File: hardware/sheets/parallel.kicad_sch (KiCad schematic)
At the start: 18 parts, among them J1 DB25_Pins, U1 74HCT374, U10 74HCT32, U11 74HCT32, U2 74HCT374, U3 74HCT244, U4 74HCT245, U5 74HCT244, U6 74HCT138, U7 74HCT08, U8 74HCT08, U9 74HCT04

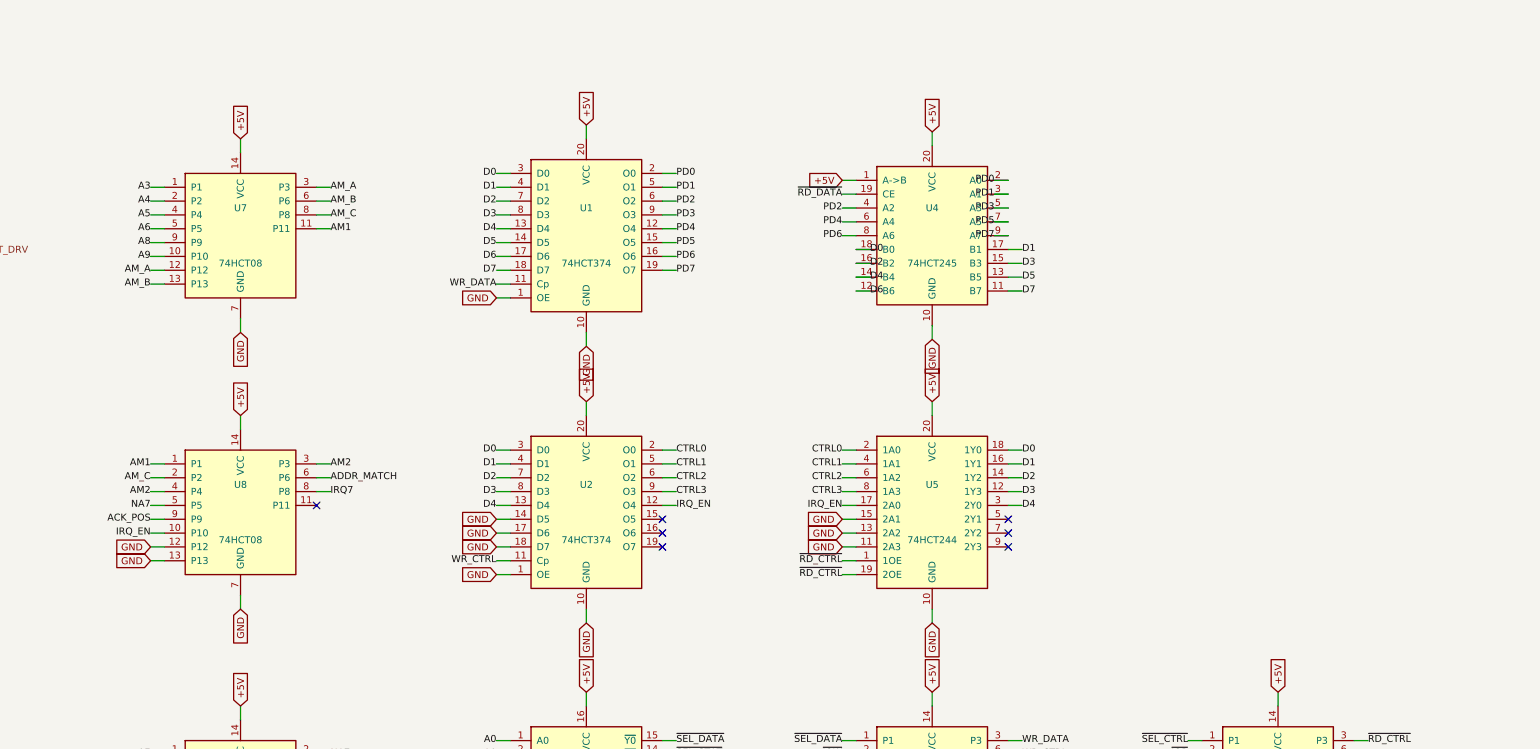
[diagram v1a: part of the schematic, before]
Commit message: Fix all low-severity + toolchain design-review findings
Low:
- LPT IRQ7 via tri-state '125 (NAND-enabled ack pulse) - shareable line
- card_com JP2 IRQ strap follows the base-address strap (was IRQ4-only)
- Supervisor USB-A VBUS fused (500mA polyfuse)
- card_isatest: DUT_PWR_EN moved to the control '595 (addr shifts can't
  glitch DUT power); '165s -> 74HC grade (HCT needs VCC 4.5-5.5V)
- /3 duty comments corrected; U13 marked load-bearing inverting buffer
- RTC AS hold-path bench note; duplicate ~RD stub removed
- mxbus PRIV_DECODE emptied (Y5 never leaves cpu_core)

Toolchain:
- build.py/build_cards return real exit codes, failing on structural ERC
  (endpoint_off_grid/unconnected_wire_endpoint/multiple_net_names) or a
  failed netlist export
- KiCad paths resolved via mxsch.kicad_cli()/kicad_symdir() (env, PATH,
  snap `current`) - no pinned snap revision anywhere
- Deterministic UUIDs (uuid5 title-seed + counter): rebuilds are
  byte-identical (verified); this rewrites every UUID once
- S-expression string escapes now round-trip (parse decodes, dump encodes)
- CLAUDE.md updated to match

The new structural gate immediately caught its own batch's bug (pull row
placed inside card_isatest's J2 pin field) - moved and re-verified.

Co-Authored-By: Claude Fable 5 <noreply@anthropic.com>
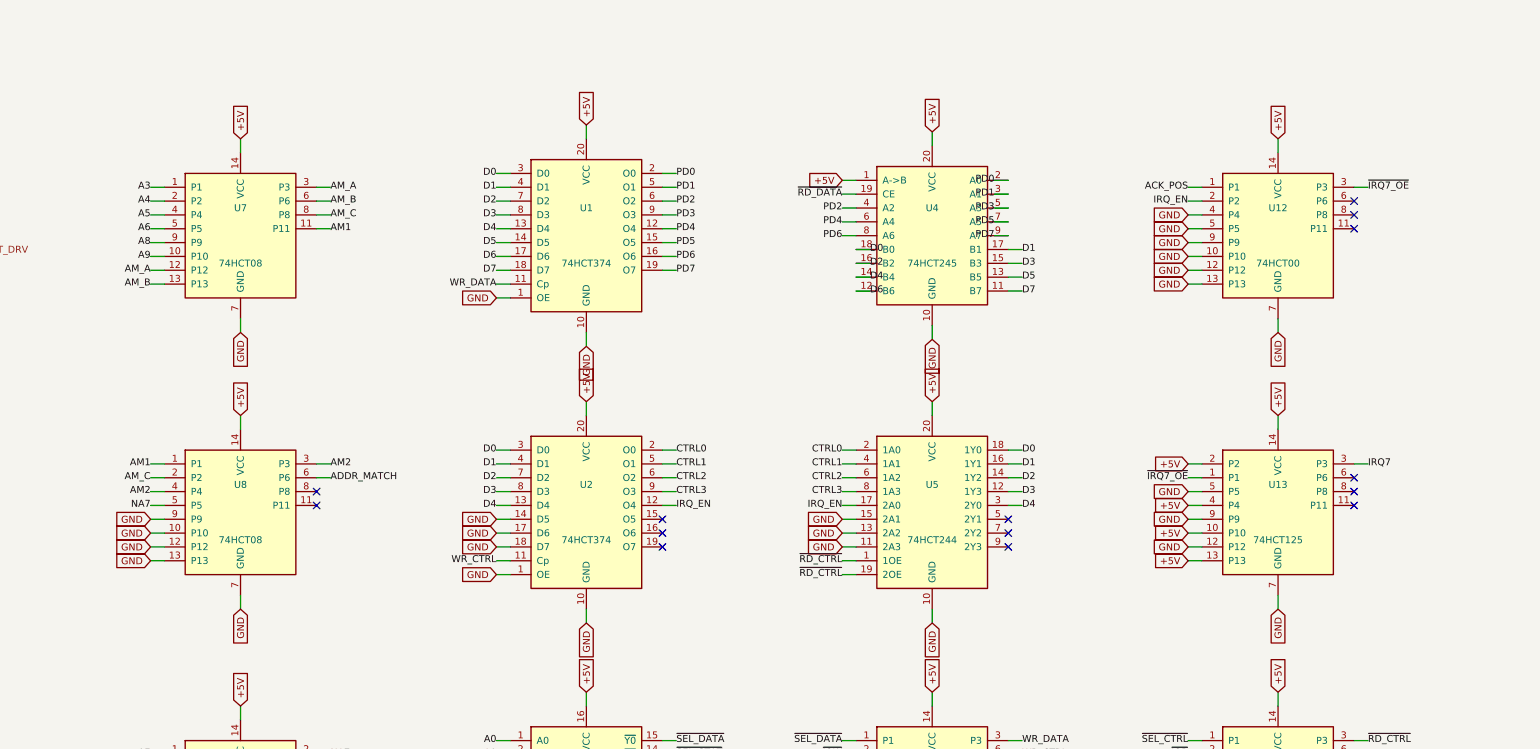
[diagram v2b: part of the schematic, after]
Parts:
- added U12: 74HCT00, symbol mini-xt:74HCT00
- added U13: 74HCT125, symbol mini-xt:74HCT125
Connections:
- net +5V: now also U12.14 (VCC), U13.10 (P10), U13.13 (P13), U13.14 (VCC), U13.2 (P2), U13.4 (P4)
- net ACK_POS: now also U12.1 (P1); no longer U8.9 (P9)
- net GND: now also U8.10 (P10), U8.9 (P9), U12.10 (P10), U12.12 (P12), U12.13 (P13), U12.4 (P4), U12.5 (P5), U12.7 (GND), U12.9 (P9), U13.12 (P12), U13.5 (P5), U13.7 (GND), U13.9 (P9)
- net IRQ7: now also U13.3 (P3); no longer U8.8 (P8)
- net IRQ_EN: now also U12.2 (P2); no longer U8.10 (P10)
- new net ~{IRQ7_OE}: U12.3 (P3), U13.1 (P1)
- no-connect marks 15 -> 22

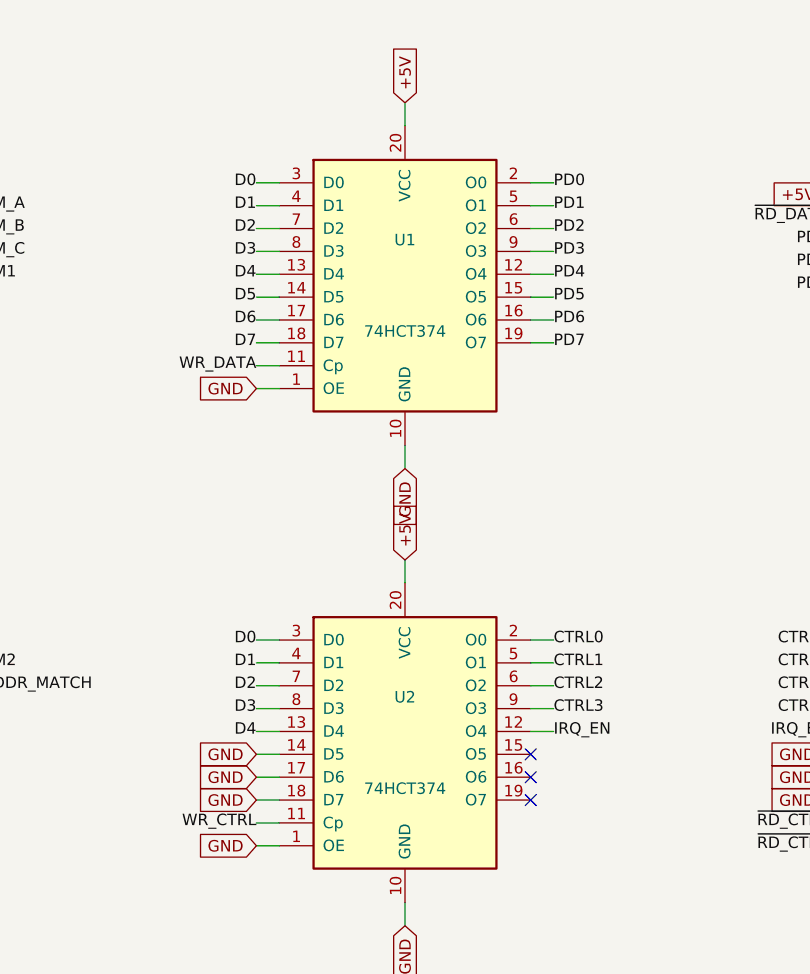
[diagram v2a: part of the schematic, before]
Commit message: JLCPCB sourcing pass: verify pinouts, LCSC part numbers, SMD build
Custom-symbol verification (open-questions Q5 resolved):
- MAX3241 symbol was wrong on nearly every pin and used MAX3243-style
  control names; regenerated to the real SSOP-28 pinout (SHDN#/EN#/
  R1OUTB/R2OUTB) and com_port rewired -- EN# must be GROUNDED (the old
  ~FORCEON-high would have disabled the receivers on real silicon)
- DS12C887 symbol wrong on 4 pins (DS=17, RESET#=18, IRQ#=19, SQW=23)

Sourcing (every part checked against the JLC DB; ~45 line items):
- New tools/parts.py maps (lib_id, value) -> LCSC; build.py applies it as
  an 'LCSC Part Num' property on every component (384 across the project)
- Sheets stay generic; stock-forced substitutions bound in the map:
  '374->'574 (parallel rewired), '163->'161, '157->HC157 (+HCT-buffered
  3.3V selects, I0/I1 swapped), '02->HC02, TCM809->MCP809, 2N3904->MMBT3904
- bus_mcu address counters moved to the 3.3V domain (HC161 on 3V3_BUS,
  loaded from MCU-side MD0-7; HCT244s read the 3.3V outputs at TTL Vih)
- 14.318 XOs are 3.3V-only parts: powered from 3V3, squared up via spare
  HCT gates (cpu_core U13, card_isatest U19)
- COM baud reference is now a 1.8432MHz crystal on the 16C550's XIN/XOUT
  (3.3V-only oscillators vs a 5V-only soft card)
- Supervisor QSPI header replaced with a real W25Q128JVSIQ
- Socket policy (fab installs sockets): V20 DIP-40, SRAM DIP-32 (no 5V
  512Kx8 SRAM at JLC at all), DS12C887 DIP-24, female headers for modules

Docs: CLAUDE.md fabrication-constraints section (SMD, 100x100mm, generic-
symbols rule, voltage-domain rule); README + hardware/README fab notes;
notes/jlcpcb-sourcing.md (decisions, thin-stock flags, not-at-JLC list);
stale questions-sidecar.md collapsed to its supersession record.

Rebuilt motherboard + cards: structural ERC 0, byte-identical rebuilds.

Co-Authored-By: Claude Fable 5 <noreply@anthropic.com>
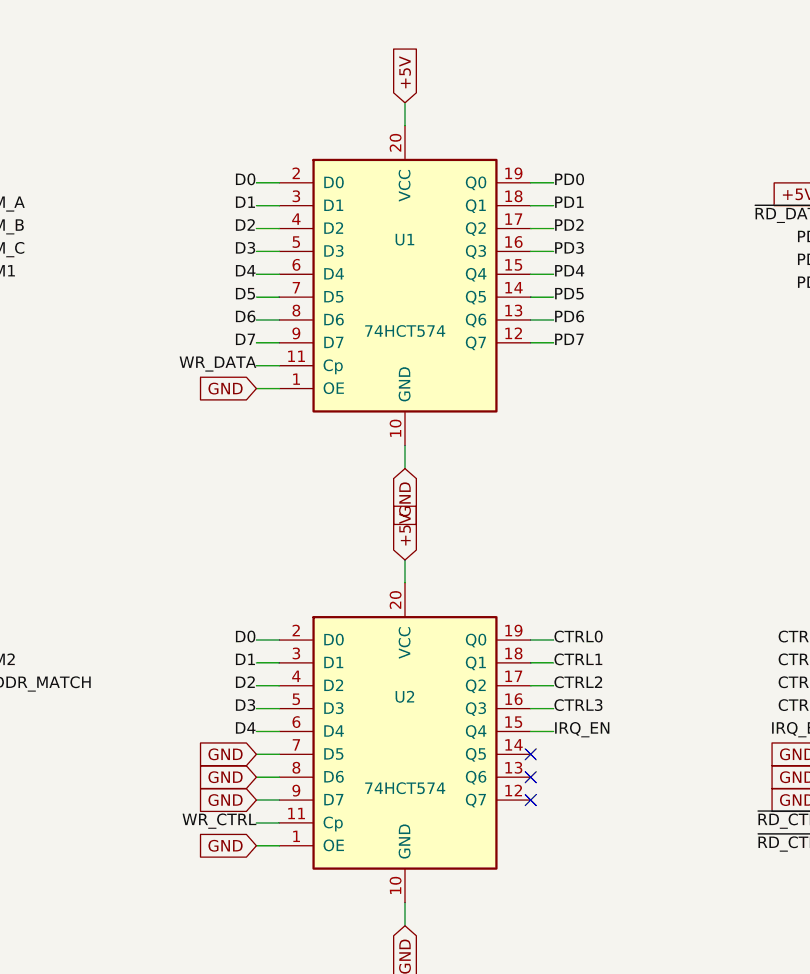
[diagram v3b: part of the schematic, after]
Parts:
- removed U1, U2: 74HCT374, symbol mini-xt:74HCT374
- added U1, U2: 74HCT574, symbol mini-xt:74HCT574
- C1, C2, C3, C4, C5, C6: LCSC Part Num (none) -> C14663
- J1: LCSC Part Num (none) -> C5400534
- U10, U11: LCSC Part Num (none) -> C5985
- U12: LCSC Part Num (none) -> C282337
- U13: LCSC Part Num (none) -> C5962
- U3, U5: LCSC Part Num (none) -> C5978
- U4: LCSC Part Num (none) -> C5979
- U6: LCSC Part Num (none) -> C5965
- U7, U8: LCSC Part Num (none) -> C5959
- U9: LCSC Part Num (none) -> C672096
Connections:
- net +5V: now also U1.20 (VCC), U2.20 (VCC)
- net CTRL0: now also U2.19 (Q0)
- net CTRL1: now also U2.18 (Q1)
- net CTRL2: now also U2.17 (Q2)
- net CTRL3: now also U2.16 (Q3)
- net D0: now also U1.2 (D0), U2.2 (D0)
- net D1: now also U1.3 (D1), U2.3 (D1)
- net D2: now also U1.4 (D2), U2.4 (D2)
- net D3: now also U1.5 (D3), U2.5 (D3)
- net D4: now also U1.6 (D4), U2.6 (D4)
- net D5: now also U1.7 (D5)
- net D6: now also U1.8 (D6)
- net D7: now also U1.9 (D7)
- net GND: now also U1.1 (OE), U1.10 (GND), U2.1 (OE), U2.10 (GND), U2.7 (D5), U2.8 (D6), U2.9 (D7)
- net IRQ_EN: now also U2.15 (Q4)
- net PD0: now also U1.19 (Q0)
- net PD1: now also U1.18 (Q1)
- net PD2: now also U1.17 (Q2)
- net PD3: now also U1.16 (Q3)
- net PD4: now also U1.15 (Q4)
- net PD5: now also U1.14 (Q5)
- net PD6: now also U1.13 (Q6)
- net PD7: now also U1.12 (Q7)
- net WR_CTRL: now also U2.11 (Cp)
- net WR_DATA: now also U1.11 (Cp)
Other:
- title: Parallel port (LPT1) -- 74HCT374/244/245 @ 0x378 + DB25 -> Parallel port (LPT1) -- 74HCT574/244/245 @ 0x378 + DB25
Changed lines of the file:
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@@
 	(paper "A3")
 	(title_block
-		(title "Parallel port (LPT1) -- 74HCT374/244/245 @ 0x378 + DB25")
+		(title "Parallel port (LPT1) -- 74HCT574/244/245 @ 0x378 + DB25")
 		(date "")
 		(rev "1")
@@
 			)
 		)
+		(property "LCSC Part Num" "C5959"
+			(at 76.2 76.2 0)
+			(effects
+				(font
+					(size 1.27 1.27)
+				)
+				(hide yes)
+			)
+		)
 		(pin "1"
 		)
@@
 			)
 		)
+		(property "LCSC Part Num" "C5959"
+			(at 76.2 127 0)
+			(effects
+				(font
+					(size 1.27 1.27)
+				)
+				(hide yes)
+			)
+		)
 		(pin "1"
 		)
@@
 			)
 		)
+		(property "LCSC Part Num" "C672096"
+			(at 76.2 177.8 0)
+			(effects
+				(font
+					(size 1.27 1.27)
+				)
+				(hide yes)
+			)
+		)
 		(pin "1"
 		)
@@
 			)
 		)
+		(property "LCSC Part Num" "C282337"
+			(at 266.7 76.2 0)
+			(effects
+				(font
+					(size 1.27 1.27)
+				)
+				(hide yes)
+			)
+		)
 		(pin "1"
 		)
@@
 			)
 		)
+		(property "LCSC Part Num" "C5962"
+			(at 266.7 127 0)
+			(effects
+				(font
+					(size 1.27 1.27)
+				)
+				(hide yes)
+			)
+		)
 		(pin "2"
 		)
@@
 			)
 		)
+		(property "LCSC Part Num" "C5965"
+			(at 139.7 177.8 0)
+			(effects
+				(font
+					(size 1.27 1.27)
+				)
+				(hide yes)
+			)
+		)
 		(pin "1"
 		)
@@
 			)
 		)
+		(property "LCSC Part Num" "C5985"
+			(at 203.2 177.8 0)
+			(effects
+				(font
+					(size 1.27 1.27)
+				)
+				(hide yes)
+			)
+		)
 		(pin "1"
 		)
@@
 			)
 		)
+		(property "LCSC Part Num" "C5985"
+			(at 266.7 177.8 0)
+			(effects
+				(font
+					(size 1.27 1.27)
+				)
+				(hide yes)
+			)
+		)
 		(pin "1"
 		)
@@
 	)
 	(symbol
-		(lib_id "mini-xt:74HCT374")
+		(lib_id "mini-xt:74HCT574")
 		(at 139.7 76.2 0)
 		(unit 1)
@@
 			)
 		)
-		(property "Value" "74HCT374"
+		(property "Value" "74HCT574"
 			(at 139.7 81.28 0)
 			(effects
@@
 			)
 		)
+		(property "LCSC Part Num" "C6001"
+			(at 139.7 76.2 0)
+			(effects
+				(font
+					(size 1.27 1.27)
+				)
+				(hide yes)
+			)
+		)
+		(pin "2"
+		)
 		(pin "3"
 		)
 		(pin "4"
 		)
-		(pin "7"
-		)
-		(pin "8"
+		(pin "5"
 		)
-		(pin "13"
+		(pin "6"
 		)
-		(pin "14"
+		(pin "7"
 		)
-		(pin "17"
+		(pin "8"
 		)
-		(pin "18"
+		(pin "9"
 		)
 		(pin "11"
@@
 		(pin "1"
 		)
-		(pin "2"
-		)
-		(pin "5"
+		(pin "19"
 		)
-		(pin "6"
+		(pin "18"
 		)
-		(pin "9"
+		(pin "17"
 		)
-		(pin "12"
+		(pin "16"
 		)
 		(pin "15"
 		)
-		(pin "16"
+		(pin "14"
 		)
-		(pin "19"
+		(pin "13"
+		)
+		(pin "12"
 		)
 		(pin "20"
@@
 			)
 		)
+		(property "LCSC Part Num" "C5979"
+			(at 203.2 76.2 0)
+			(effects
+				(font
+					(size 1.27 1.27)
+				)
+				(hide yes)
+			)
+		)
 		(pin "1"
 		)
@@
 	)
 	(symbol
-		(lib_id "mini-xt:74HCT374")
+		(lib_id "mini-xt:74HCT574")
 		(at 139.7 127 0)
 		(unit 1)
@@
 			)
 		)
-		(property "Value" "74HCT374"
+		(property "Value" "74HCT574"
 			(at 139.7 132.08 0)
 			(effects
@@
 			)
 		)
+		(property "LCSC Part Num" "C6001"
+			(at 139.7 127 0)
+			(effects
+				(font
+					(size 1.27 1.27)
+				)
+				(hide yes)
+			)
+		)
+		(pin "2"
+		)
 		(pin "3"
 		)
 		(pin "4"
 		)
-		(pin "7"
-		)
-		(pin "8"
+		(pin "5"
 		)
-		(pin "13"
+		(pin "6"
 		)
-		(pin "14"
+		(pin "7"
 		)
-		(pin "17"
+		(pin "8"
 		)
-		(pin "18"
+		(pin "9"
 		)
 		(pin "11"
@@
 		(pin "1"
 		)
-		(pin "2"
-		)
-		(pin "5"
+		(pin "19"
 		)
-		(pin "6"
+		(pin "18"
 		)
-		(pin "9"
+		(pin "17"
 		)
-		(pin "12"
+		(pin "16"
 		)
 		(pin "15"
 		)
-		(pin "16"
+		(pin "14"
 		)
-		(pin "19"
+		(pin "13"
+		)
+		(pin "12"
 		)
 		(pin "20"
@@
 			)
 		)
+		(property "LCSC Part Num" "C5978"
+			(at 203.2 127 0)
+			(effects
+				(font
+					(size 1.27 1.27)
+				)
+				(hide yes)
+			)
+		)
 		(pin "2"
 		)
@@
 			)
 		)
+		(property "LCSC Part Num" "C5978"
+			(at 203.2 228.6 0)
+			(effects
+				(font
+					(size 1.27 1.27)
+				)
+				(hide yes)
+			)
+		)
 		(pin "2"
 		)
@@
 			)
 		)
+		(property "LCSC Part Num" "C5400534"
+			(at 355.6 127 0)
+			(effects
+				(font
+					(size 1.27 1.27)
+				)
+				(hide yes)
+			)
+		)
 		(pin "13"
 		)
@@
 			)
 		)
+		(property "LCSC Part Num" "C14663"
+			(at 76.2 264.16 0)
+			(effects
+				(font
+					(size 1.27 1.27)
+				)
+				(hide yes)
+			)
+		)
 		(pin "1"
 		)
@@
 			)
 		)
+		(property "LCSC Part Num" "C14663"
+			(at 116.84 264.16 0)
+			(effects
+				(font
+					(size 1.27 1.27)
+				)
+				(hide yes)
+			)
+		)
 		(pin "1"
 		)
@@
 			)
 		)
+		(property "LCSC Part Num" "C14663"
+			(at 157.48 264.16 0)
+			(effects
+				(font
+					(size 1.27 1.27)
+				)
+				(hide yes)
+			)
+		)
 		(pin "1"
 		)
@@
 			)
 		)
+		(property "LCSC Part Num" "C14663"
+			(at 198.12 264.16 0)
+			(effects
+				(font
+					(size 1.27 1.27)
+				)
+				(hide yes)
+			)
+		)
 		(pin "1"
 		)
@@
 			)
 		)
+		(property "LCSC Part Num" "C14663"
+			(at 238.76 264.16 0)
+			(effects
+				(font
+					(size 1.27 1.27)
+				)
+				(hide yes)
+			)
+		)
 		(pin "1"
 		)
@@
 			(at 279.4 264.16 0)
 			(effects
+				(font
+					(size 1.27 1.27)
+				)
+				(hide yes)
+			)
+		)
+		(property "LCSC Part Num" "C14663"
+			(at 279.4 264.16 0)
+			(effects
